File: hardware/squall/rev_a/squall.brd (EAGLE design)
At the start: 25.4 x 24 mm, 38 parts, among them J1 HIROSE-DF40C-10DP-0.4V, J2 HIROSE-DF40C-10DP-0.4V, J3 MICRO_USB_B_JST_MC5BR3-M404-4S, J4 TC2030-JLINK-NL, U1 NRF51822QF, U2 FT232RQ, X1 16MHz, X2 ABS05-32.768KHZ-9-T

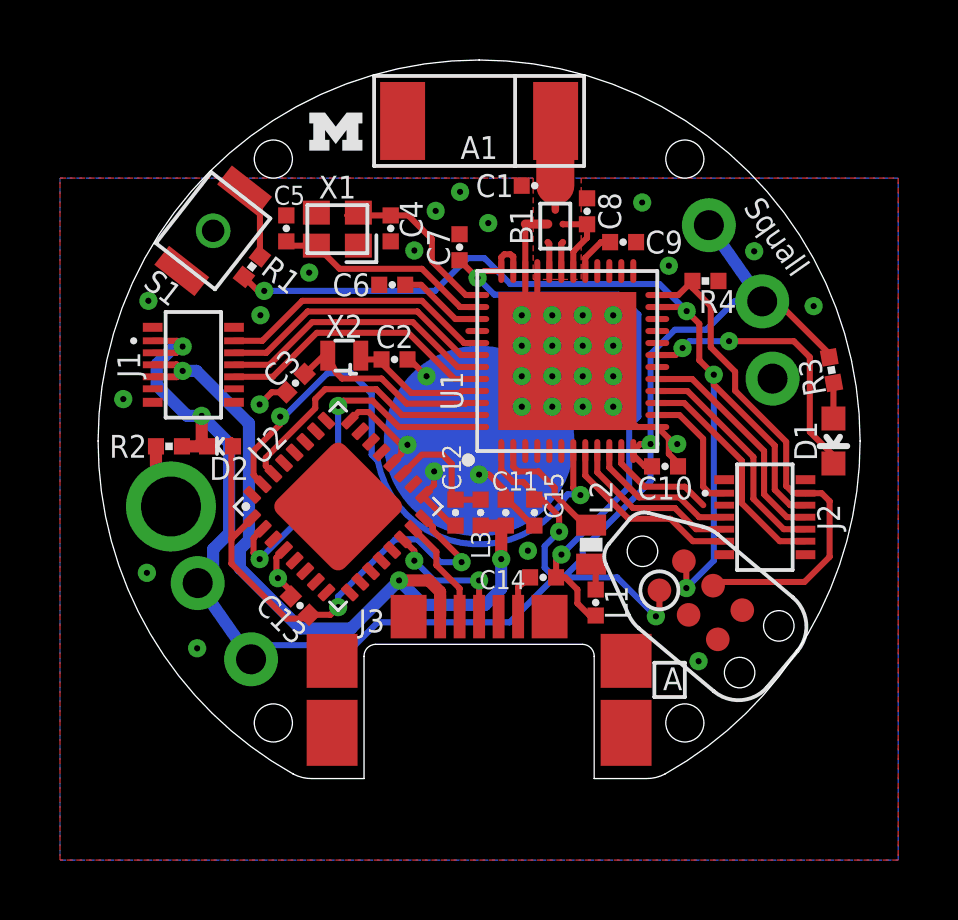
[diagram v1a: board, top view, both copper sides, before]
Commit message: fixes: battery location and ftdi
- rotated battery clip to hopefully not conflict with mounting holes
- connected test on FTDI to gnd
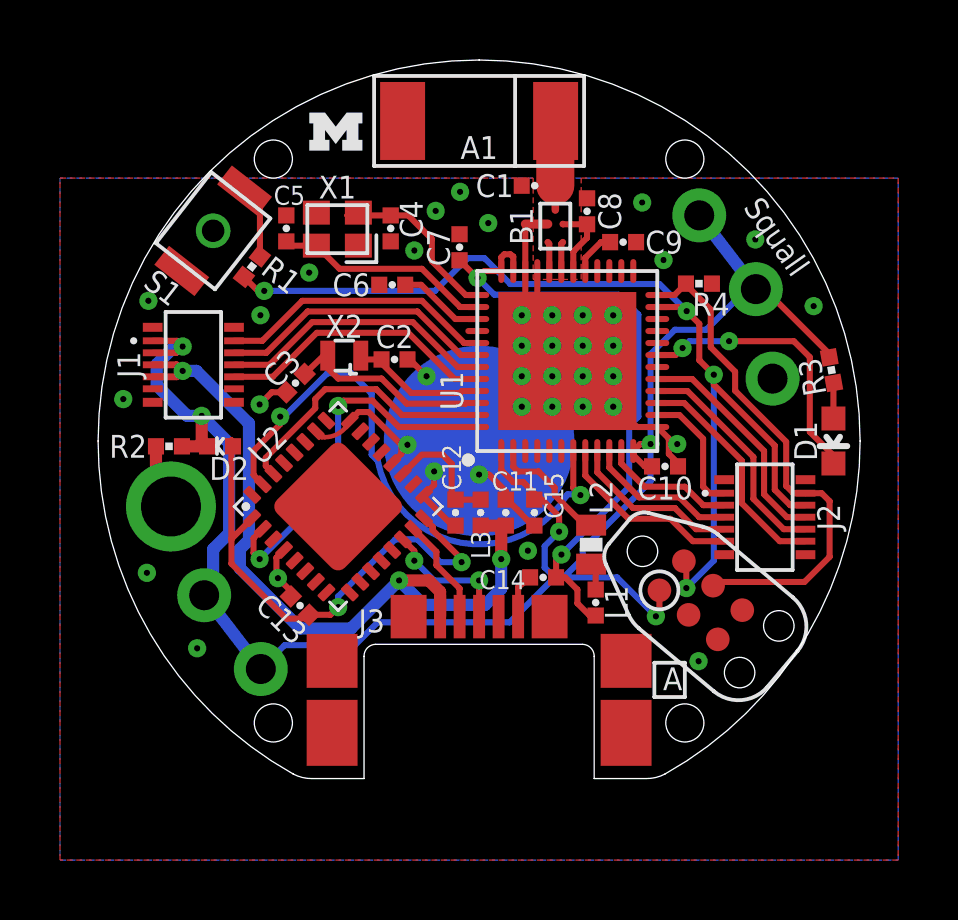
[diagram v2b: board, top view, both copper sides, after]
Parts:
- moved R4 0.23 mm to (20.0, 17.9)
- turned BAT1 to 322.5 degrees
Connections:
- removed net P07: U1.11
- removed net P12: U1.18
- removed net P21: U1.40
- net GND: now also U2.26
- net SCL: now also U1.11
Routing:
- net SCL: track 0.00 -> 4.42 mm
- net P07: track 3.73 -> 0.00 mm
- net GND: track 26.1 -> 27.6 mm
